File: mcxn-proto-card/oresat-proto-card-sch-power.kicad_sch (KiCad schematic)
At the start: 90 parts, among them Q1 DMP2240UDM, Q2 DMP3050LVT-7, Q7 MOSFET-PCH-SOT23-6, Q8 PMV45EN, Q9 PMV45EN, U10 TPS62111RSA, U11 MIC842LYC5, U12 MIC842LYC5, U2 MAX7310, U3 TS5A21366DCUR, U6 MAX4211

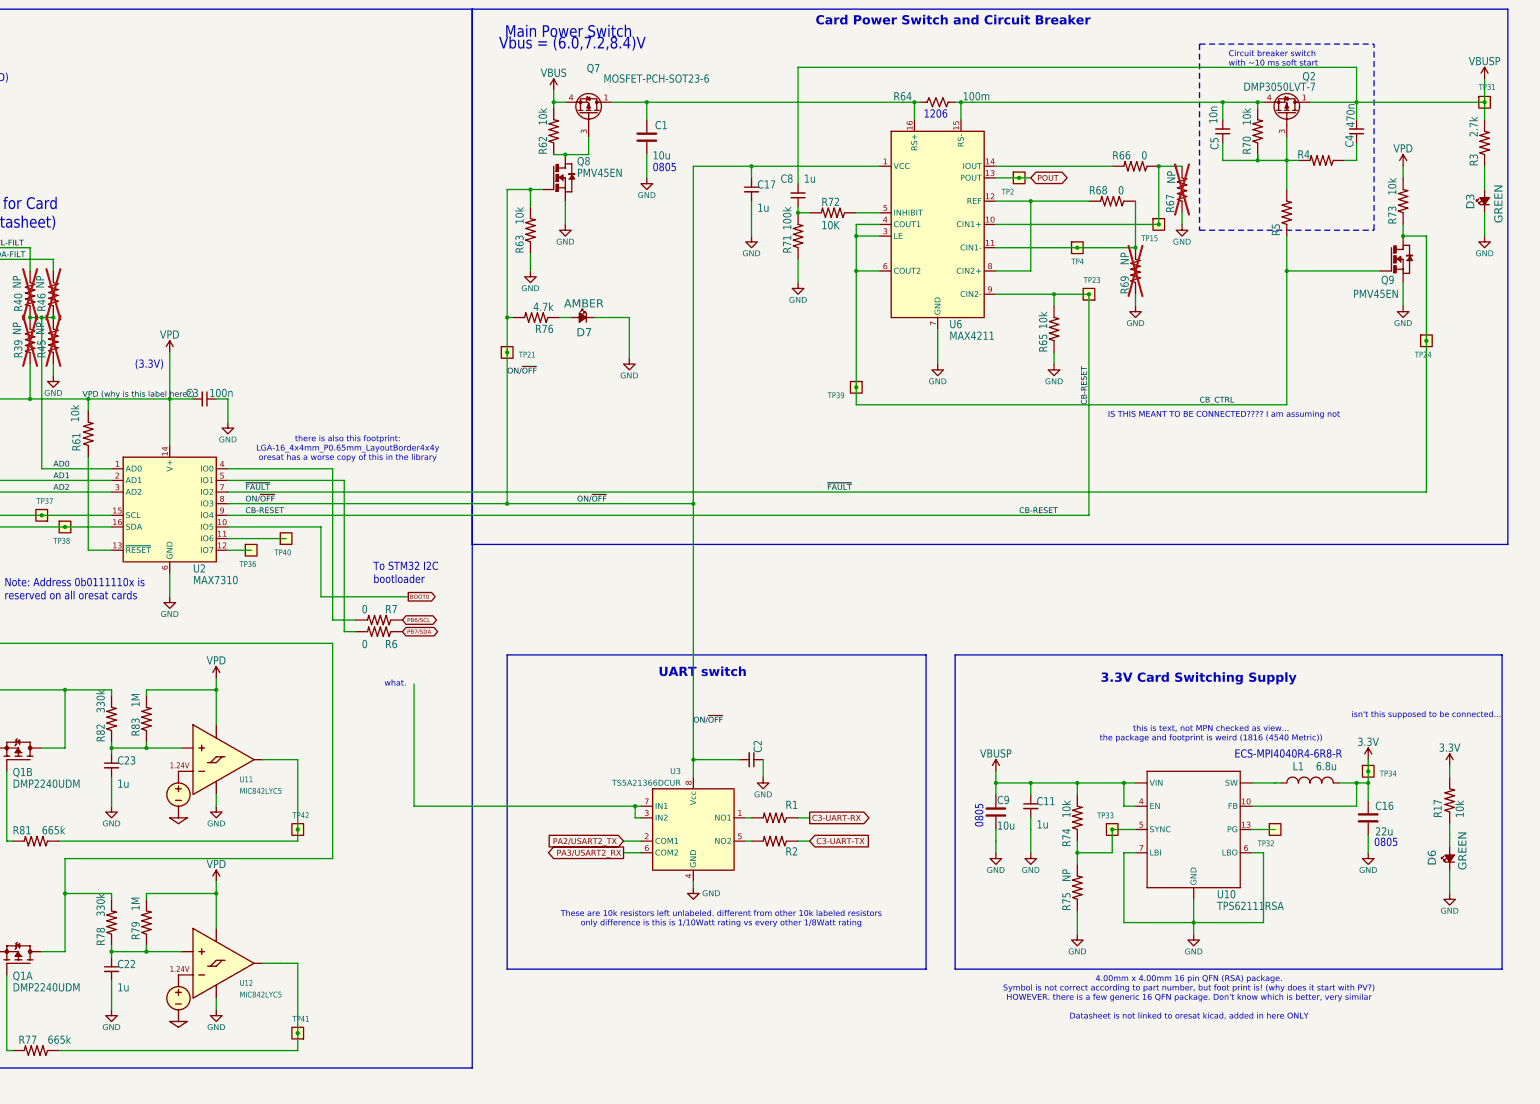
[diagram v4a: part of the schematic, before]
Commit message: Eagle libraries replaced, scheatic and layout clean up cont.
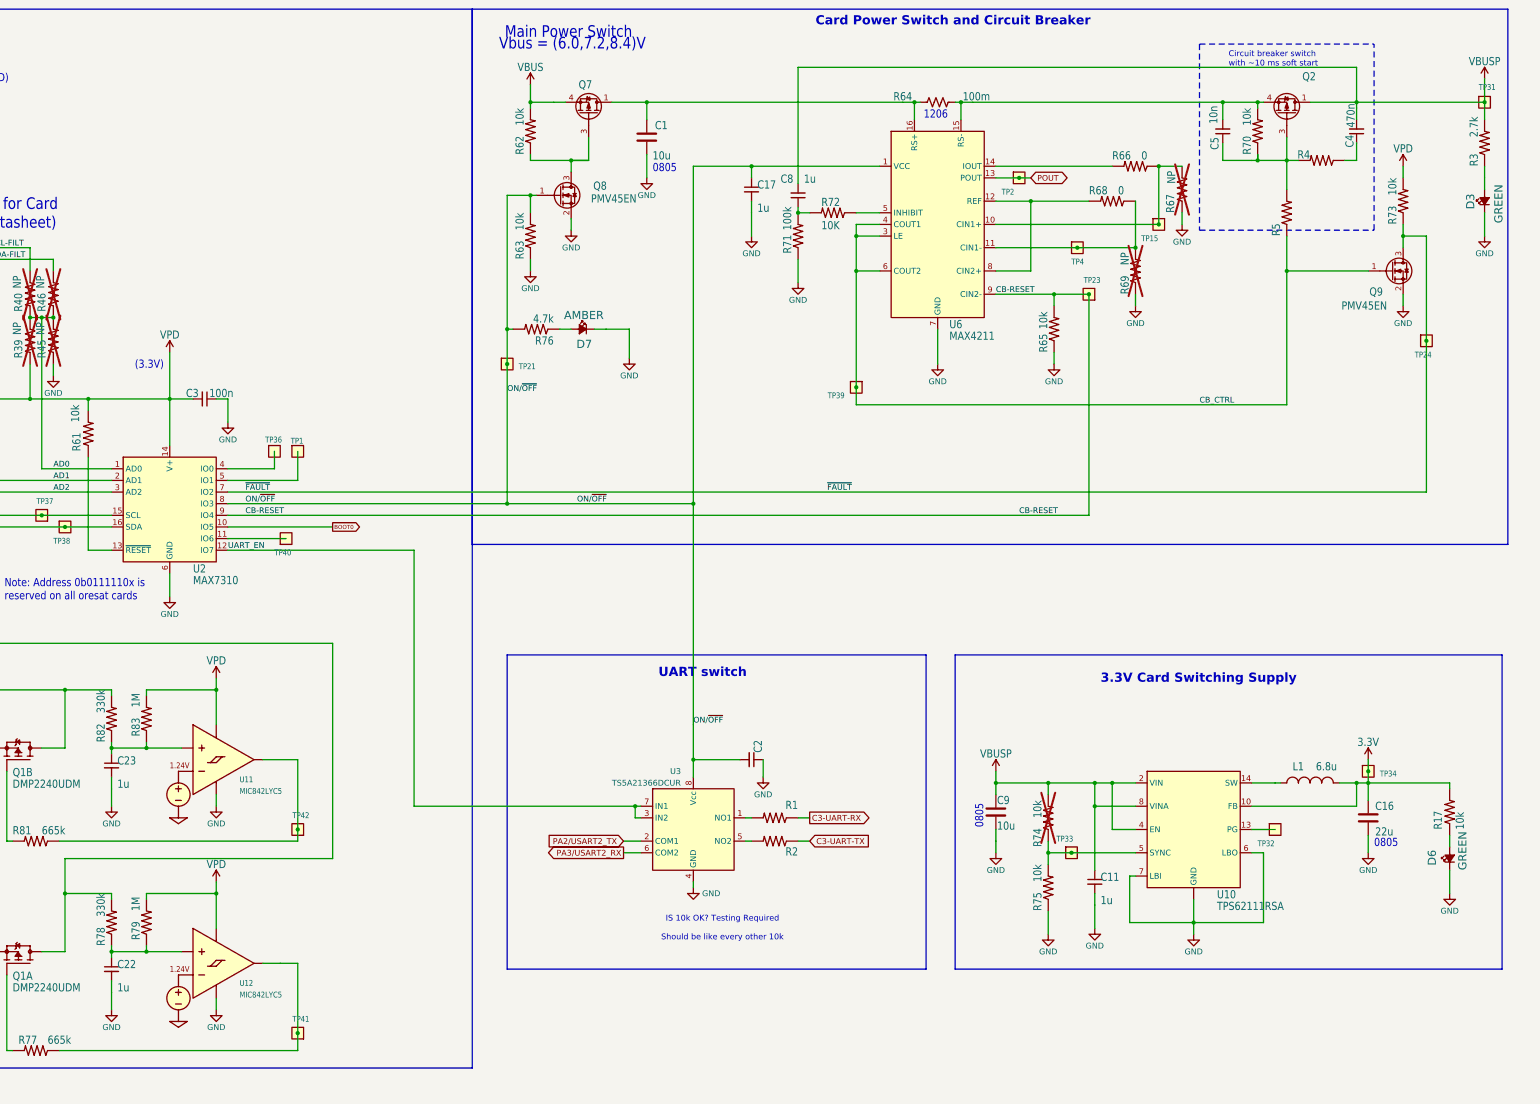
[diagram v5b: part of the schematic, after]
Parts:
- removed R6, R7: 0, oresat-passives:0603-C-NOSILK, symbol oresat-passives:R-US
- added TP1: Test-Point, oresat-misc:TestPoint-0.75mm-th, symbol oresat-misc:Test-Point-0.75mm-th
- Q8, Q9: symbol oresat-proto-card-eagle-import:PMV45EN -> Transistor_FET:Q_NMOS_GSD
- R74: now not fitted
- R75: value NP -> 10k
- U10: symbol oresat-proto-card-eagle-import:TPS6211X -> oresat-ics:TPS6211X
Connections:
- net CB-RESET: no longer Q9.1 (G), R5.1, TP39.1, U6.3 (LE), U6.4 (COUT1), U6.6 (COUT2)
- net at U2.5 (IO1): now also TP1.1
- net UART_EN: now reaches U3.3 (IN2), U3.7 (IN1)
- net UART_EN: now also U2.12 (IO7)
- net at TP36.1: now also U2.4 (IO0); no longer U2.12 (IO7)
- new net CB_CTRL: Q9.1 (G), R5.1, TP39.1, U6.3 (LE), U6.4 (COUT1), U6.6 (COUT2)
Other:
- note added: "IS 10k OK? Testing Required Should be like every other 10k"
- note removed: "4.00mm x 4.00mm 16 pin QFN (RSA) package. Symbol is not correct according to part number, but foot print is! (why does it start with PV?) HOWEVER. there is a few generic 16 QFN package. Don't know which is better, very similar Datasheet is not linked to oresat kicad, added in here ONLY"
- note removed: "ECS-MPI4040R4-6R8-R"
- note removed: "IS THIS MEANT TO BE CONNECTED???? I am assuming not"
- note removed: "These are 10k resistors left unlabeled. different from other 10k labeled resistors only difference is this is 1/10Watt rating vs every other 1/8Watt rating"
- note removed: "To STM32 I2C bootloader"
- note removed: "isn't this supposed to be connected..."
- note removed: "there is also this footprint: LGA-16_4x4mm_P0.65mm_LayoutBorder4x4y oresat has a worse copy of this in the library"
- note removed: "this is text, not MPN checked as view... the package and footprint is weird (1816 (4540 Metric))"
- note removed: "what."
- moved on the sheet: C11, D7, R17, R62, R63, R75, R76, TP21, TP33, TP36

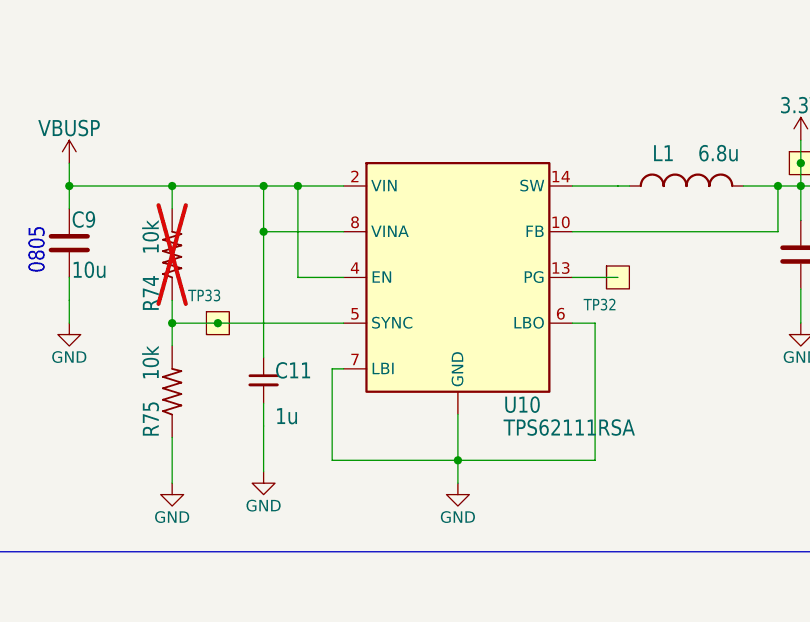
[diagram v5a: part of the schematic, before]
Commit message: Updated TPS62111RSA
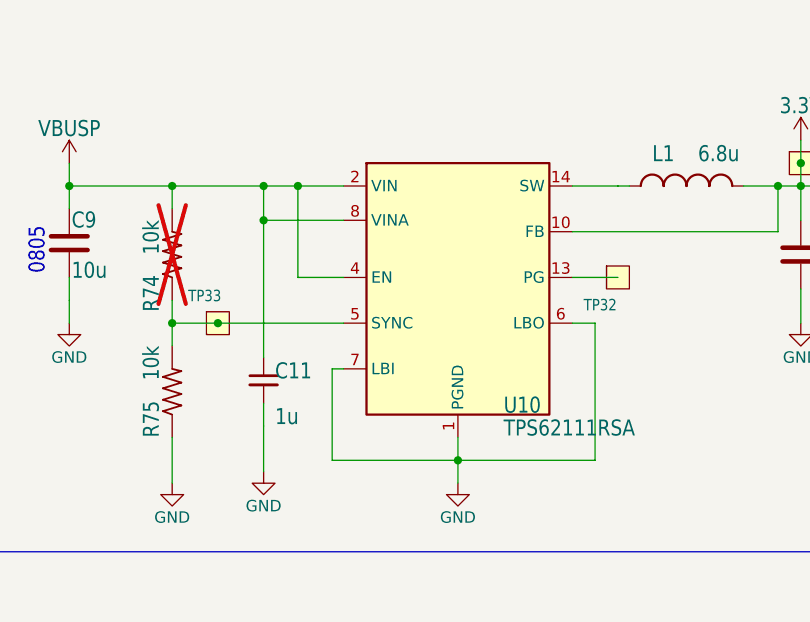
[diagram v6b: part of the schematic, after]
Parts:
- Q8: footprint oresat-proto-card:SOT23 -> oresat-ics:SOT23
- U10: footprint oresat-proto-card:S-PVQFN-16 -> Package_DFN_QFN:QFN-16-1EP_4x4mm_P0.65mm_EP2.15x2.15mm
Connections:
- net GND renamed AGND
- net AGND: no longer U10.PAD (GND)
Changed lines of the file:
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@@
 	)
 	(junction
+		(at 321.31 187.96)
+		(diameter 0)
+		(color 0 0 0 0)
+	)
+	(junction
 		(at 73.66 100.33)
 		(diameter 0)
@@
 	)
 	(junction
-		(at 321.31 189.23)
-		(diameter 0)
-		(color 0 0 0 0)
-	)
-	(junction
 		(at 320.04 77.47)
 		(diameter 0)
@@
 	(wire
 		(pts
-			(xy 330.2 189.23) (xy 321.31 189.23)
+			(xy 330.2 187.96) (xy 321.31 187.96)
 		)
 		(stroke
@@
 	(wire
 		(pts
-			(xy 321.31 189.23) (xy 321.31 203.2)
+			(xy 321.31 187.96) (xy 321.31 203.2)
 		)
 		(stroke
@@
 	(wire
 		(pts
-			(xy 342.9 209.55) (xy 342.9 214.63)
-		)
-		(stroke
-			(width 0.1524)
-			(type solid)
-		)
-	)
-	(wire
-		(pts
 			(xy 356.87 35.56) (xy 358.14 35.56)
 		)
@@
 	(wire
 		(pts
-			(xy 76.2 82.55) (xy 73.66 82.55)
+			(xy 321.31 187.96) (xy 321.31 184.15)
 		)
 		(stroke
-			(width 0.1524)
-			(type solid)
+			(width 0)
+			(type default)
 		)
 	)
 	(wire
 		(pts
-			(xy 62.23 220.98) (xy 49.53 220.98)
+			(xy 76.2 82.55) (xy 73.66 82.55)
 		)
 		(stroke
@@
 	(wire
 		(pts
-			(xy 43.18 69.85) (xy 63.5 69.85)
+			(xy 62.23 220.98) (xy 49.53 220.98)
 		)
 		(stroke
@@
 	(wire
 		(pts
-			(xy 360.68 184.15) (xy 361.95 184.15)
+			(xy 43.18 69.85) (xy 63.5 69.85)
 		)
 		(stroke
-			(width 0)
-			(type default)
+			(width 0.1524)
+			(type solid)
 		)
 	)
 	(wire
 		(pts
-			(xy 321.31 189.23) (xy 321.31 184.15)
+			(xy 360.68 184.15) (xy 361.95 184.15)
 		)
 		(stroke
@@
 	(wire
 		(pts
+			(xy 342.9 212.09) (xy 342.9 214.63)
+		)
+		(stroke
+			(width 0)
+			(type default)
+		)
+	)
+	(wire
+		(pts
 			(xy 269.24 72.39) (xy 274.32 72.39)
 		)
@@
 			)
 		)
-		(property "Footprint" "oresat-proto-card:S-PVQFN-16"
+		(property "Footprint" "Package_DFN_QFN:QFN-16-1EP_4x4mm_P0.65mm_EP2.15x2.15mm"
 			(at 342.9 191.77 0)
 			(effects
@@
 		(pin "6"
 		)
-		(pin "PAD"
-		)
 		(pin "13"
 		)
@@
 		(pin "3"
 		)
-		(pin "8"
-		)
 		(instances
 			(project "oresat-proto-card"
@@
 			)
 		)
-		(property "Footprint" "oresat-proto-card:SOT23"
+		(property "Footprint" "oresat-ics:SOT23"
 			(at 209.55 53.34 0)
 			(effects
